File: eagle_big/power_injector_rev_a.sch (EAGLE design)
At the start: 23 parts, among them J2 A00-108-220-450, J3 A00-108-220-450, X1 22-23-2041, X10 22-23-2041, X11 22-23-2041, X12 22-23-2041, X13 22-23-2041, X14 22-23-2041, X15 22-23-2041, X16 22-23-2041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

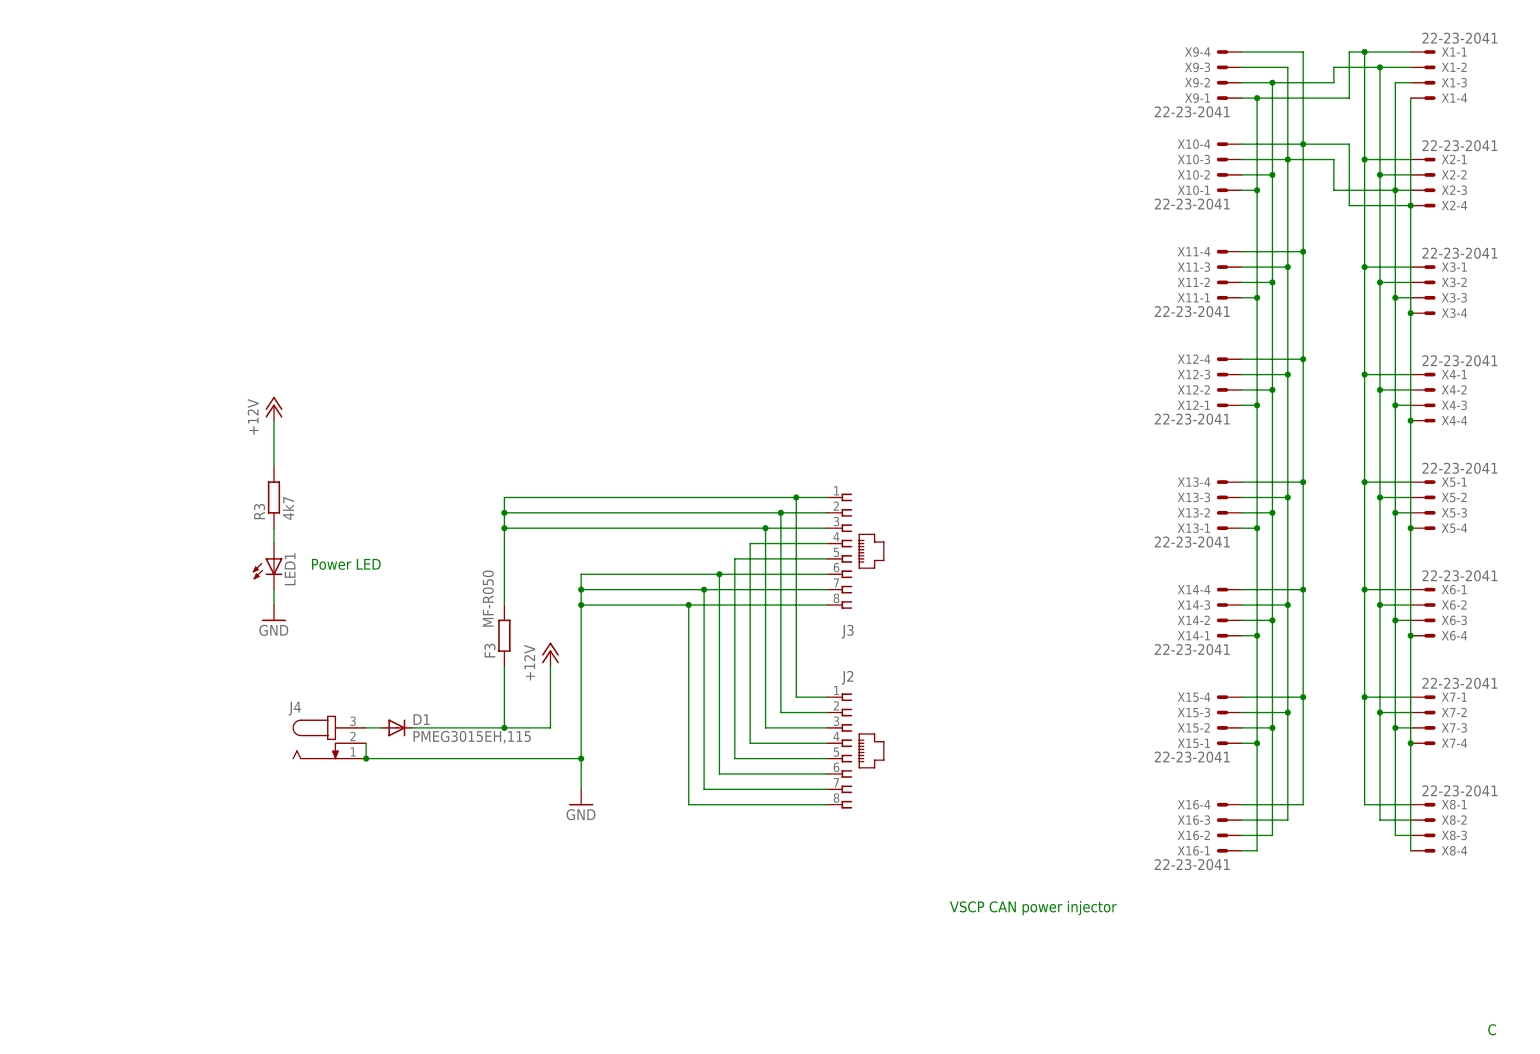
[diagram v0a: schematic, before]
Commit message: Added terminators and changed connection sequence
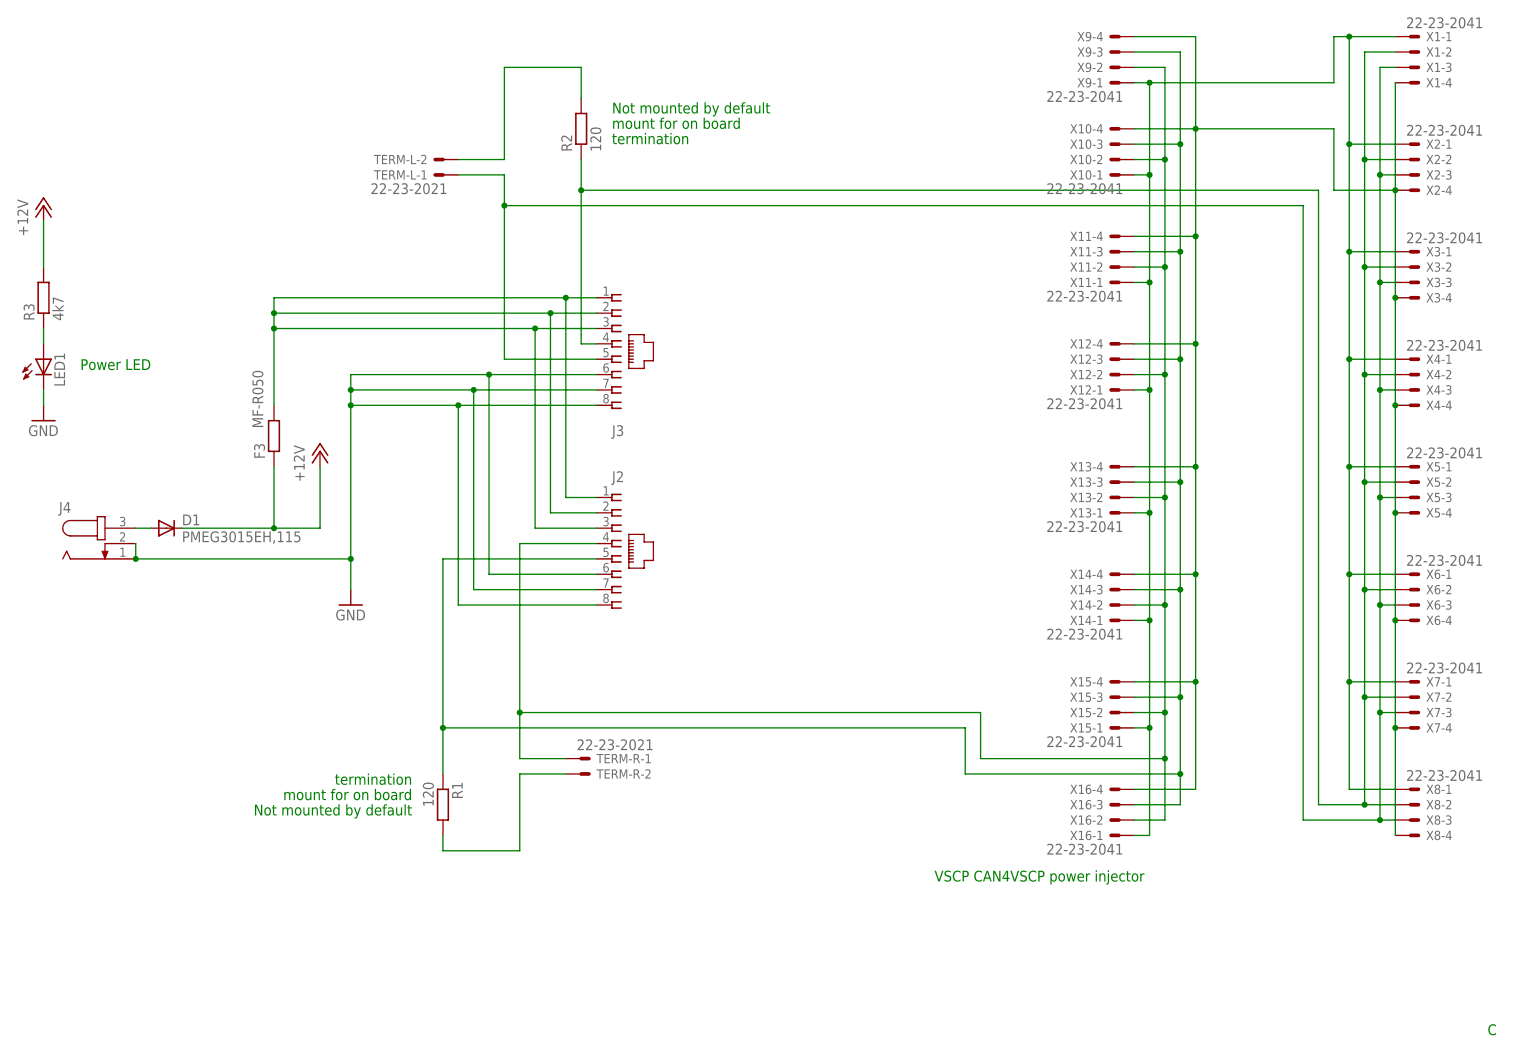
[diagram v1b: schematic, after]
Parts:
- added R1, R2: 120, rcl:R-EU_R0805
- added TERM-L, TERM-R: 22-23-2021, con-molex:22-23-2021
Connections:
- new net N$11: R2.2, TERM-L-2.S
- new net N$3: R1.2, TERM-R-2.S
- net CANH: now also R2.1, TERM-R-1.S
- net CANL: now also R1.1, TERM-L-1.S
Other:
- note added: "Not mounted by default"
- note added: "VSCP CAN4VSCP power injector"
- note added: "mount for on board"
- note added: "termination"
- note removed: "VSCP CAN power injector"
- moved on the sheet: D1, F3, J2, J3, J4, LED1, R3, X1-1, X1-2, X1-3, X1-4, X10-1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
